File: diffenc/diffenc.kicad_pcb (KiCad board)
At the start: 4 copper layers, 70 x 30 mm, 14 parts, among them J1 RJ45_Shielded, U1 AS5047, U2 SN65LVDT14

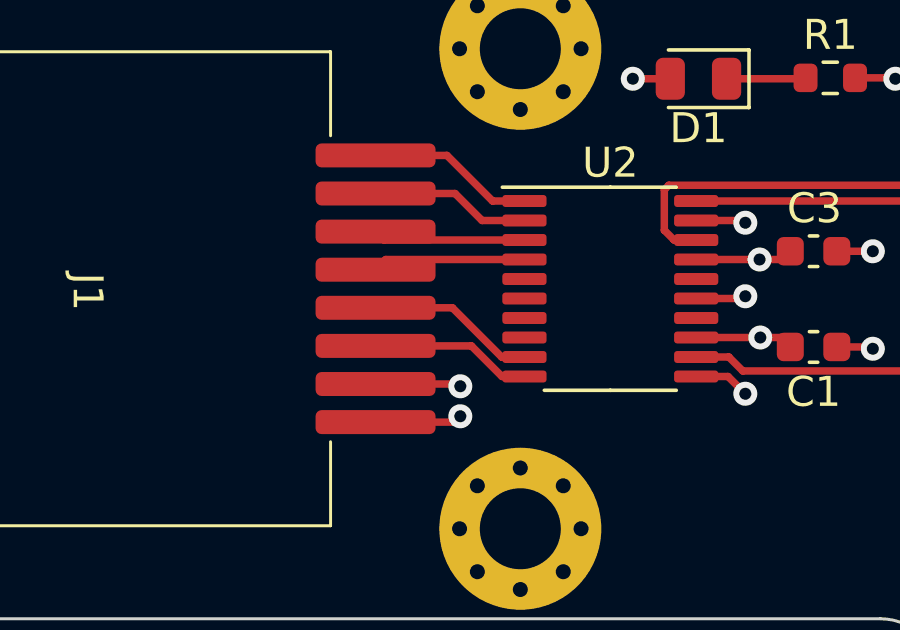
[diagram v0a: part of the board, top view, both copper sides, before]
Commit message: diffenc: fix pairs
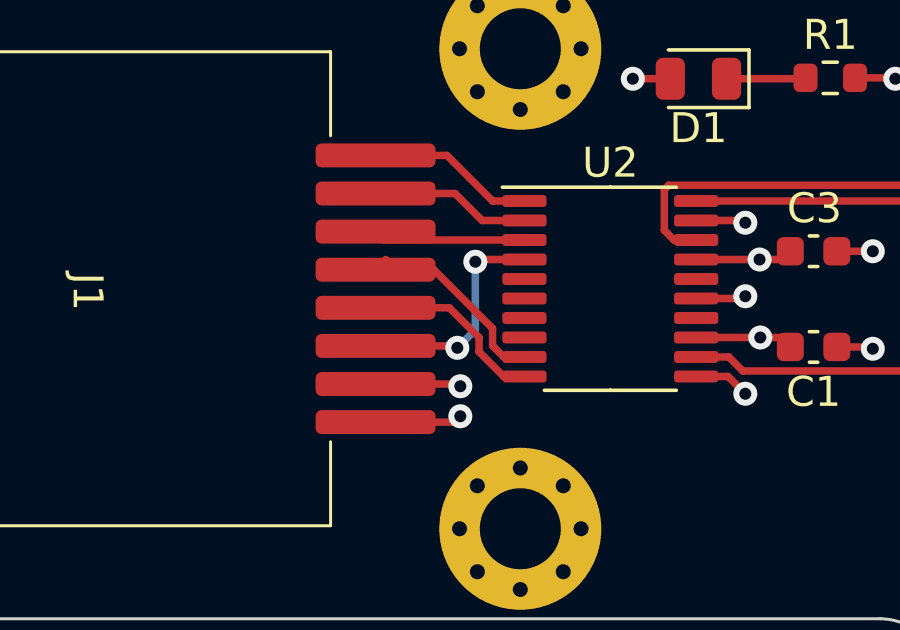
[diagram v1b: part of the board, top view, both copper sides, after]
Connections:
- J1 pad 4: Net-(U2-2B) -> Net-(U2-5Y)
- J1 pad 5: Net-(U2-5Y) -> Net-(U2-5Z)
- J1 pad 6: Net-(U2-5Z) -> Net-(U2-2B)
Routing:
- net Net-(U2-2B): track 5.10 -> 7.54 mm, vias 0 -> 2
- net Net-(U2-5Y): track 5.64 -> 6.99 mm
- net Net-(U2-5Z): track 5.38 -> 6.19 mm
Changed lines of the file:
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@@
       (net 6 "Net-(U2-2A)") (pintype "passive") (thermal_bridge_angle 45))
     (pad "4" smd roundrect (at -0.635 -10.9 270) (size 0.8 4) (layers "F.Cu" "F.Paste" "F.Mask") (roundrect_rratio 0.25)
+      (net 8 "Net-(U2-5Y)") (pintype "passive") (thermal_bridge_angle 45))
+    (pad "5" smd roundrect (at 0.635 -10.9 270) (size 0.8 4) (layers "F.Cu" "F.Paste" "F.Mask") (roundrect_rratio 0.25)
+      (net 9 "Net-(U2-5Z)") (pintype "passive") (thermal_bridge_angle 45))
+    (pad "6" smd roundrect (at 1.905 -10.9 270) (size 0.8 4) (layers "F.Cu" "F.Paste" "F.Mask") (roundrect_rratio 0.25)
       (net 7 "Net-(U2-2B)") (pintype "passive") (thermal_bridge_angle 45))
-    (pad "5" smd roundrect (at 0.635 -10.9 270) (size 0.8 4) (layers "F.Cu" "F.Paste" "F.Mask") (roundrect_rratio 0.25)
-      (net 8 "Net-(U2-5Y)") (pintype "passive") (thermal_bridge_angle 45))
-    (pad "6" smd roundrect (at 1.905 -10.9 270) (size 0.8 4) (layers "F.Cu" "F.Paste" "F.Mask") (roundrect_rratio 0.25)
-      (net 9 "Net-(U2-5Z)") (pintype "passive") (thermal_bridge_angle 45))
     (pad "7" smd roundrect (at 3.175 -10.9 270) (size 0.8 4) (layers "F.Cu" "F.Paste" "F.Mask") (roundrect_rratio 0.25)
       (net 1 "+3V3") (pintype "passive") (thermal_bridge_angle 45))
@@
   (segment (start 72.455 63.375) (end 77.1375 63.375) (width 0.25) (layer "F.Cu") (net 6))
   (segment (start 72.175 63.095) (end 72.455 63.375) (width 0.25) (layer "F.Cu") (net 6))
-  (segment (start 72.175 64.365) (end 72.515 64.025) (width 0.25) (layer "F.Cu") (net 7))
-  (segment (start 72.515 64.025) (end 77.1375 64.025) (width 0.25) (layer "F.Cu") (net 7))
-  (segment (start 76.377462 67.275) (end 77.1375 67.275) (width 0.25) (layer "F.Cu") (net 8))
-  (segment (start 74.737462 65.635) (end 76.377462 67.275) (width 0.25) (layer "F.Cu") (net 8))
-  (segment (start 72.175 65.635) (end 74.737462 65.635) (width 0.25) (layer "F.Cu") (net 8))
-  (segment (start 75.371066 66.905) (end 76.391066 67.925) (width 0.25) (layer "F.Cu") (net 9))
-  (segment (start 72.175 66.905) (end 75.371066 66.905) (width 0.25) (layer "F.Cu") (net 9))
-  (segment (start 76.391066 67.925) (end 77.1375 67.925) (width 0.25) (layer "F.Cu") (net 9))
+  (segment (start 74.9005 66.968698) (end 74.836802 66.905) (width 0.25) (layer "F.Cu") (net 7))
+  (segment (start 75.5745 64.025) (end 77.1375 64.025) (width 0.25) (layer "F.Cu") (net 7))
+  (segment (start 74.836802 66.905) (end 72.175 66.905) (width 0.25) (layer "F.Cu") (net 7))
+  (segment (start 75.5 64.0995) (end 75.5745 64.025) (width 0.25) (layer "F.Cu") (net 7))
+  (via (at 75.5 64.0995) (size 0.8) (drill 0.4) (layers "F.Cu" "B.Cu") (net 7))
+  (via (at 74.9005 66.968698) (size 0.8) (drill 0.4) (layers "F.Cu" "B.Cu") (net 7))
+  (segment (start 74.9005 66.968698) (end 75.5 66.369198) (width 0.25) (layer "B.Cu") (net 7))
+  (segment (start 75.5 66.369198) (end 75.5 64.0995) (width 0.25) (layer "B.Cu") (net 7))
+  (segment (start 76.448959 67.275) (end 77.1375 67.275) (width 0.25) (layer "F.Cu") (net 8))
+  (segment (start 74.115 64.365) (end 76.075 66.325) (width 0.25) (layer "F.Cu") (net 8))
+  (segment (start 72.175 64.365) (end 72.515 64.025) (width 0.25) (layer "F.Cu") (net 8))
+  (segment (start 72.175 64.365) (end 74.115 64.365) (width 0.25) (layer "F.Cu") (net 8))
+  (segment (start 76.075 66.325) (end 76.075 66.901041) (width 0.25) (layer "F.Cu") (net 8))
+  (segment (start 76.075 66.901041) (end 76.448959 67.275) (width 0.25) (layer "F.Cu") (net 8))
+  (segment (start 76.448959 67.925) (end 77.1375 67.925) (width 0.25) (layer "F.Cu") (net 9))
+  (segment (start 72.175 65.635) (end 74.635 65.635) (width 0.25) (layer "F.Cu") (net 9))
+  (segment (start 74.635 65.635) (end 75.625 66.625) (width 0.25) (layer "F.Cu") (net 9))
+  (segment (start 75.625 66.625) (end 75.625 67.101041) (width 0.25) (layer "F.Cu") (net 9))
+  (segment (start 75.625 67.101041) (end 76.448959 67.925) (width 0.25) (layer "F.Cu") (net 9))
   (segment (start 81.95 61.55) (end 101.6375 61.55) (width 0.25) (layer "F.Cu") (net 10))
   (segment (start 101.6375 61.55) (end 103.1375 63.05) (width 0.25) (layer "F.Cu") (net 10))

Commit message: diffenc: diff pairs
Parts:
- moved C1 1.90 mm to (85.0, 66.3), turned to 90 degrees
- moved C3 1.84 mm to (85.0, 63.3), turned to -90 degrees
- moved C2 0.87 mm to (110.8, 64.4), turned to -90 degrees
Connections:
- net Net-(U2-1A) renamed /LVD1_P
- net Net-(U2-1B) renamed /LVD1_N
- J1 pad 3: Net-(U2-2A) -> +3V3
- J1 pad 4: Net-(U2-5Y) -> /LVD2_P
- J1 pad 5: Net-(U2-5Z) -> /LVD2_N
- J1 pad 6: Net-(U2-2B) -> GND
- J1 pad 7: +3V3 -> /LVD5_P
- J1 pad 8: GND -> /LVD5_N
- U2 pad 10: Net-(U2-5Z) -> /LVD5_N
- U2 pad 3: Net-(U2-2A) -> /LVD2_P
- U2 pad 4: Net-(U2-2B) -> /LVD2_N
- U2 pad 9: Net-(U2-5Y) -> /LVD5_P
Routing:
- net Net-(U2-2B): track 7.54 -> 0.00 mm, vias 2 -> 0
- net Net-(U2-5Y): track 6.99 -> 0.00 mm
- net Net-(U2-5Z): track 6.19 -> 0.00 mm
- net GND: track 18.7 -> 12.5 mm, vias 11 -> 9
- net /LVD2_P: track 0.00 -> 5.71 mm
- net /LVD2_N: track 0.00 -> 5.71 mm
- net /LVD5_P: track 0.00 -> 5.67 mm
- net /LVD5_N: track 0.00 -> 5.67 mm
- net Net-(U2-2A): track 5.08 -> 0.00 mm
- net +3V3: track 20.3 -> 16.3 mm
- net Net-(U1-CSn): track 24.6 -> 25.9 mm
- added copper zone on B.Cu, net GND
